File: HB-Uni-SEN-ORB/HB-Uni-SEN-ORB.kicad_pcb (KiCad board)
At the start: 2 copper layers, 55.1 x 63.7 mm, 27 parts, among them J2 BNC, U1 Arduino_Pro_Mini, U2 CC1101, U3 LM2660M, U4 LM358M_NOPB

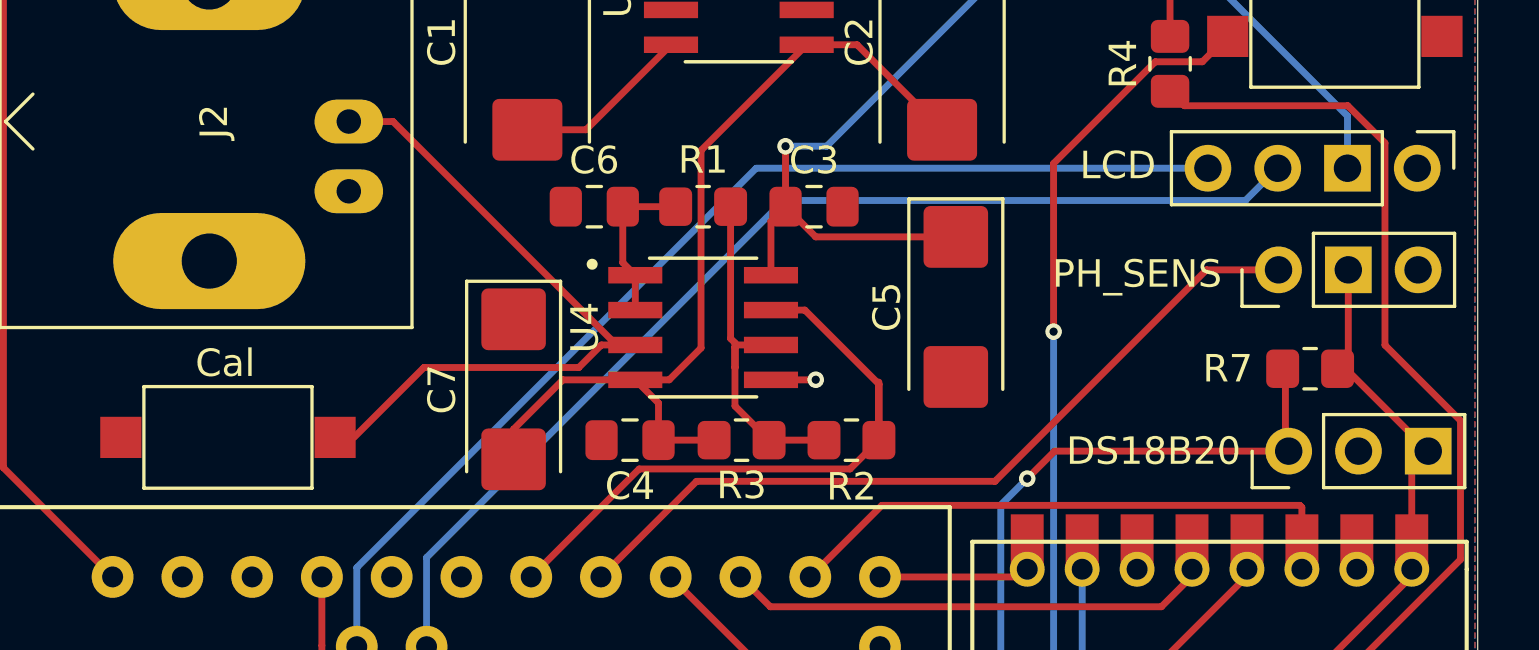
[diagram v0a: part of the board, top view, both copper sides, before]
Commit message: Add files via upload
Add I2C Pullup
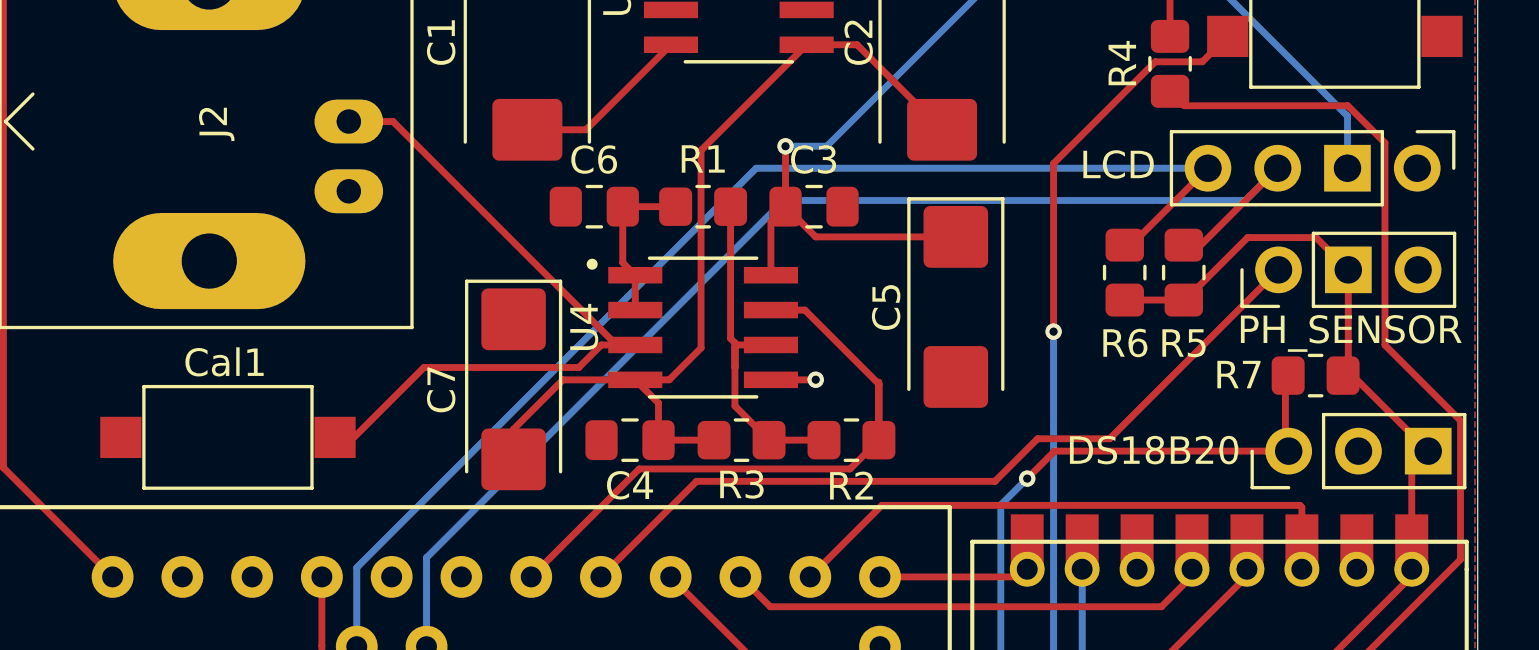
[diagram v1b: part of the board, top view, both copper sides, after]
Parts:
- added R5: 10K, Resistor_SMD:R_0805_2012Metric_Pad1.20x1.40mm_HandSolder, F.Cu at (153.8, 75.5)
- added R6: 10K, Resistor_SMD:R_0805_2012Metric_Pad1.20x1.40mm_HandSolder, F.Cu at (151.7, 75.5)
- moved R7 0.32 mm to (158.6, 79.2)
- renumbered Cal to Cal1, PH_SENS to PH_SENSOR
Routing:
- net /VCC: track 65.8 -> 75.4 mm
- net /SDA: track 40.2 -> 44.8 mm
- net /SCL: track 39.9 -> 44.1 mm
